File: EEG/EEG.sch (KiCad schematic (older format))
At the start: 46 parts, among them J1 USB_B_Micro, J2 Conn_01x08_Female, J3 Conn_01x08_Female, Q1 SS8050, Q2 SS8050, SW1 SW_Push, SW2 SW_Push, U1 AMS1117-3.3, U2 FT231XS, U3 ESP32-PICO-D4, U4 MAX7219

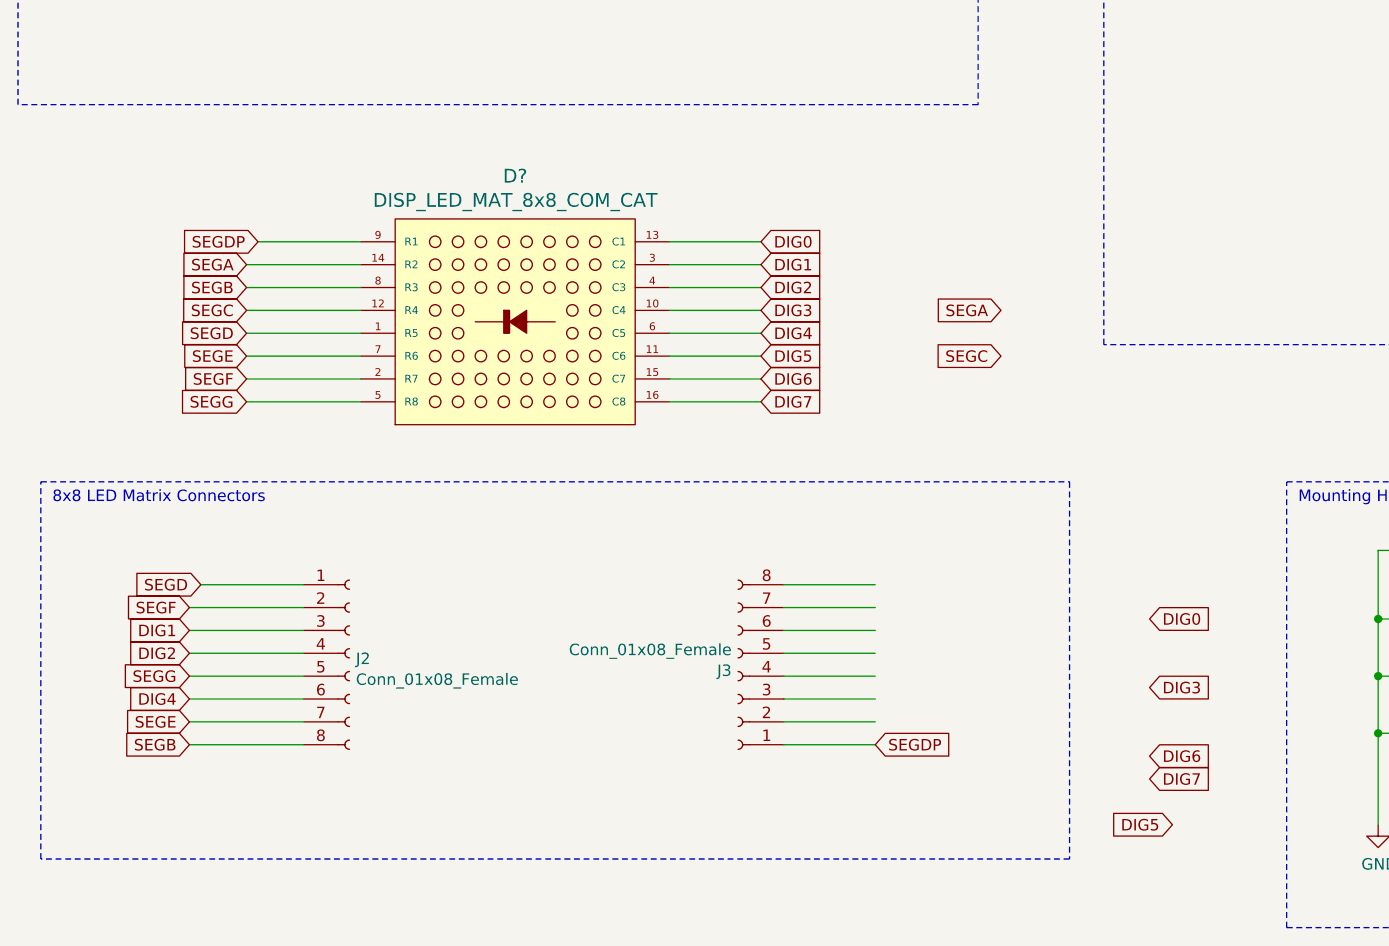
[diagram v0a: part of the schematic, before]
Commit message: updated sch for led conn
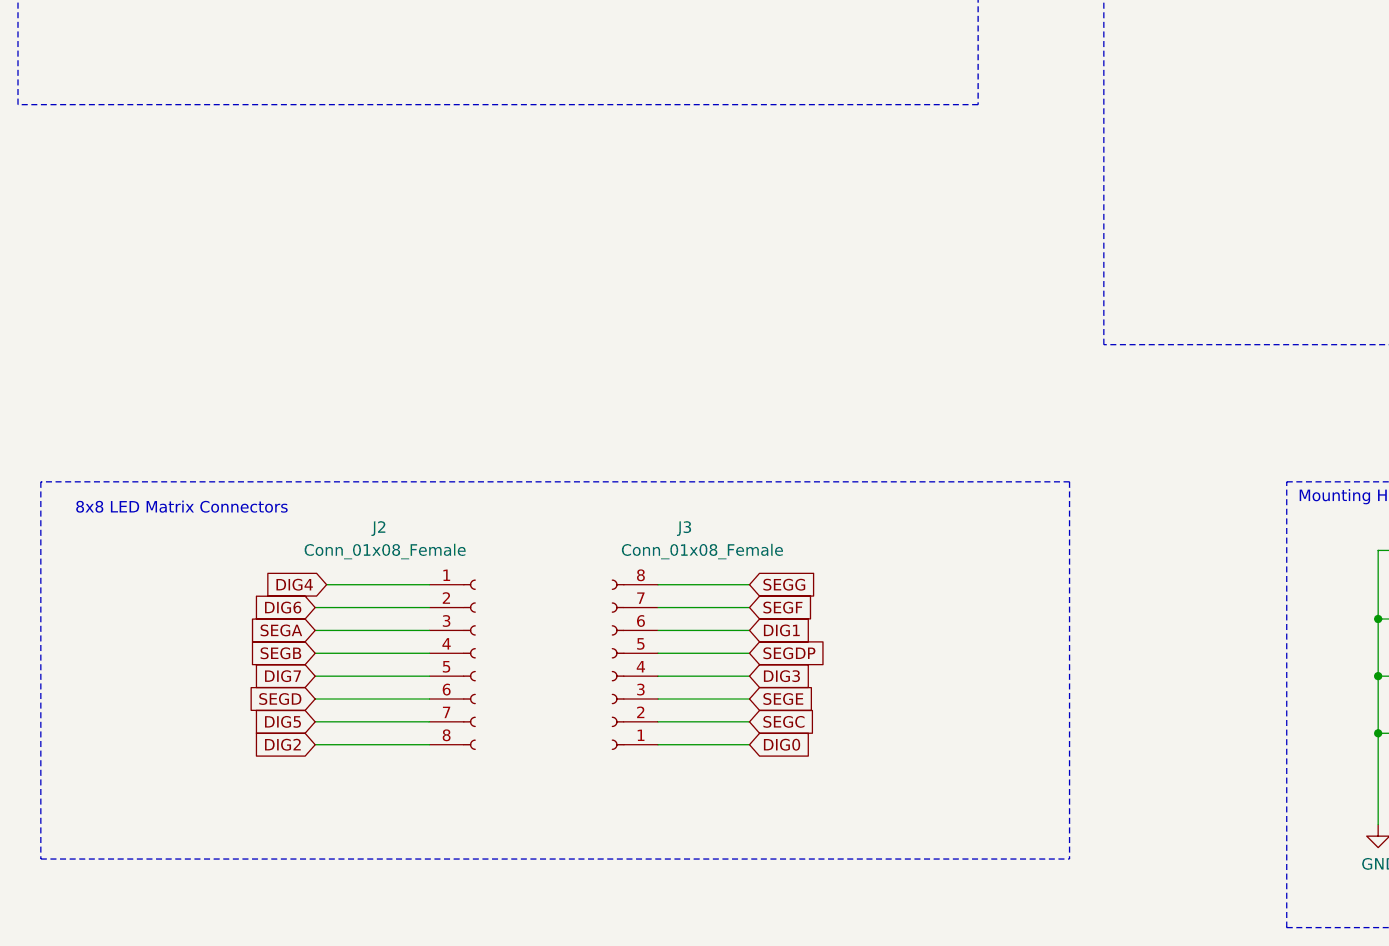
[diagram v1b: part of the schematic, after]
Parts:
- removed D?: DISP_LED_MAT_8x8_COM_CAT, symbol akn_misc:DISP_LED_MAT_8x8_COM_CAT
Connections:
- wire segments 215 -> 199
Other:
- moved on the sheet: J2, J3
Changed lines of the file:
@@
 L Connector:Conn_01x08_Female J3
 U 1 1 604BA9B3
-P 3900 9950
-F 0 "J3" H 3928 9926 50  0000 L CNN
-F 1 "Conn_01x08_Female" H 3928 9835 50  0000 L CNN
-F 2 "Connector_PinSocket_2.54mm:PinSocket_1x08_P2.54mm_Vertical" H 3900 9950 50  0001 C CNN
-F 3 "~" H 3900 9950 50  0001 C CNN
-	1    3900 9950
+P 3350 9950
+F 0 "J3" H 3000 9300 50  0000 L CNN
+F 1 "Conn_01x08_Female" H 2600 9400 50  0000 L CNN
+F 2 "Connector_PinSocket_2.54mm:PinSocket_1x08_P2.54mm_Vertical" H 3350 9950 50  0001 C CNN
+F 3 "~" H 3350 9950 50  0001 C CNN
+	1    3350 9950
 	-1   0    0    1
 $EndComp
@@
 L Connector:Conn_01x08_Female J2
 U 1 1 604BC715
-P 2200 9850
-F 0 "J2" H 2228 9826 50  0000 L CNN
-F 1 "Conn_01x08_Female" H 2228 9735 50  0000 L CNN
-F 2 "Connector_PinSocket_2.54mm:PinSocket_1x08_P2.54mm_Vertical" H 2200 9850 50  0001 C CNN
-F 3 "~" H 2200 9850 50  0001 C CNN
-	1    2200 9850
+P 2750 9850
+F 0 "J2" H 2300 10400 50  0000 L CNN
+F 1 "Conn_01x08_Female" H 2000 10300 50  0000 L CNN
+F 2 "Connector_PinSocket_2.54mm:PinSocket_1x08_P2.54mm_Vertical" H 2750 9850 50  0001 C CNN
+F 3 "~" H 2750 9850 50  0001 C CNN
+	1    2750 9850
 	1    0    0    -1
 $EndComp
@@
 Text Notes 11000 4750 0    50   ~ 0
 MAX7219 LED Matrix Driver
-Wire Notes Line
-	5350 9100 5350 10750
-Wire Notes Line
-	5350 10750 850  10750
-Wire Notes Line
-	850  10750 850  9100
-Wire Notes Line
-	850  9100 5350 9100
-Text Notes 900  9200 0    50   ~ 0
+Text Notes 1000 9250 0    50   ~ 0
 8x8 LED Matrix Connectors
 NoConn ~ 9200 4800
@@
 	1    0    0    -1
 $EndComp
-Text GLabel 1750 8150 0    50   Input ~ 0
+Wire Wire Line
+	3550 10250 3950 10250
+Wire Wire Line
+	3550 10150 3950 10150
+Wire Wire Line
+	3550 10050 3950 10050
+Wire Wire Line
+	3550 9950 3950 9950
+Wire Wire Line
+	3550 9850 3950 9850
+Wire Wire Line
+	3550 9750 3950 9750
+Wire Wire Line
+	3550 9650 3950 9650
+Wire Wire Line
+	3550 9550 3950 9550
+Text GLabel 2050 9950 0    50   Input ~ 0
+DIG7
+Text GLabel 3950 10250 2    50   Input ~ 0
+DIG0
+Text GLabel 2050 9650 0    50   Input ~ 0
+DIG6
+Text GLabel 2050 10150 0    50   Input ~ 0
+DIG5
+Text GLabel 2100 9550 0    50   Input ~ 0
+DIG4
+Text GLabel 3950 9950 2    50   Input ~ 0
+DIG3
+Text GLabel 2050 10250 0    50   Input ~ 0
+DIG2
+Text GLabel 3950 9750 2    50   Input ~ 0
+DIG1
+Text GLabel 3950 9850 2    50   Input ~ 0
+SEGDP
+Text GLabel 3950 9550 2    50   Input ~ 0
+SEGG
+Text GLabel 3950 9650 2    50   Input ~ 0
+SEGF
+Text GLabel 3950 10050 2    50   Input ~ 0
+SEGE
+Text GLabel 2050 10050 0    50   Input ~ 0
+SEGD
+Text GLabel 3950 10150 2    50   Input ~ 0
+SEGC
+Text GLabel 2050 9850 0    50   Input ~ 0
+SEGB
+Text GLabel 2050 9750 0    50   Input ~ 0
 SEGA
-Text GLabel 1750 8250 0    50   Input ~ 0
-SEGB
-Text GLabel 1750 8350 0    50   Input ~ 0
-SEGC
-Text GLabel 1750 8450 0    50   Input ~ 0
-SEGD
-Text GLabel 1750 8550 0    50   Input ~ 0
-SEGE
-Text GLabel 1750 8650 0    50   Input ~ 0
-SEGF
-Text GLabel 1750 8750 0    50   Input ~ 0
-SEGG
-Wire Wire Line
-	1750 8150 2250 8150
-Wire Wire Line
-	1750 8250 2250 8250
-Wire Wire Line
-	1750 8350 2250 8350
-Wire Wire Line
-	1750 8450 2250 8450
-Wire Wire Line
-	1750 8550 2250 8550
-Wire Wire Line
-	1750 8650 2250 8650
-Wire Wire Line
-	1750 8750 2250 8750
-Text GLabel 4000 8150 2    50   Input ~ 0
-DIG1
-Text GLabel 4000 8250 2    50   Input ~ 0
-DIG2
-Text GLabel 4000 8350 2    50   Input ~ 0
-DIG3
-Text GLabel 4000 8450 2    50   Input ~ 0
-DIG4
-Text GLabel 4000 8550 2    50   Input ~ 0
-DIG5
-Text GLabel 4000 8650 2    50   Input ~ 0
-DIG6
-Text GLabel 4000 8050 2    50   Input ~ 0
-DIG0
-Text GLabel 4000 8750 2    50   Input ~ 0
-DIG7
-Wire Wire Line
-	3600 8050 4000 8050
-Wire Wire Line
-	3600 8150 4000 8150
-Wire Wire Line
-	3600 8250 4000 8250
-Wire Wire Line
-	3600 8350 4000 8350
-Wire Wire Line
-	3600 8450 4000 8450
-Wire Wire Line
-	3600 8550 4000 8550
-Wire Wire Line
-	3600 8650 4000 8650
-Wire Wire Line
-	3600 8750 4000 8750
-Wire Wire Line
-	4100 10250 4500 10250
-Wire Wire Line
-	4100 10150 4500 10150
-Wire Wire Line
-	4100 10050 4500 10050
-Wire Wire Line
-	4100 9950 4500 9950
-Wire Wire Line
-	4100 9850 4500 9850
-Wire Wire Line
-	4100 9750 4500 9750
-Wire Wire Line
-	4100 9650 4500 9650
-Wire Wire Line
-	4100 9550 4500 9550
-Text GLabel 5700 10400 2    50   Input ~ 0
-DIG7
-Text GLabel 5700 9700 2    50   Input ~ 0
-DIG0
-Text GLabel 5700 10300 2    50   Input ~ 0
-DIG6
-Text GLabel 5800 10600 0    50   Input ~ 0
-DIG5
-Text GLabel 1500 10050 0    50   Input ~ 0
-DIG4
-Text GLabel 5700 10000 2    50   Input ~ 0
-DIG3
-Text GLabel 1500 9850 0    50   Input ~ 0
-DIG2
-Text GLabel 1500 9750 0    50   Input ~ 0
-DIG1
-Wire Wire Line
-	1550 9550 2000 9550
-Wire Wire Line
-	1500 10250 2000 10250
-Wire Wire Line
-	1500 10150 2000 10150
-Wire Wire Line
-	1500 10050 2000 10050
-Wire Wire Line
-	1500 9950 2000 9950
-Wire Wire Line
-	1500 9850 2000 9850
-Wire Wire Line
-	1500 9750 2000 9750
-Wire Wire Line
-	1500 9650 2000 9650
-Text GLabel 4500 10250 2    50   Input ~ 0
-SEGDP
-Text GLabel 1500 9950 0    50   Input ~ 0
-SEGG
-Text GLabel 1500 9650 0    50   Input ~ 0
-SEGF
-Text GLabel 1500 10150 0    50   Input ~ 0
-SEGE
-Text GLabel 1550 9550 0    50   Input ~ 0
-SEGD
-Text GLabel 5050 8550 0    50   Input ~ 0
-SEGC
-Text GLabel 1500 10250 0    50   Input ~ 0
-SEGB
-Text GLabel 5050 8350 0    50   Input ~ 0
-SEGA
-Text GLabel 1800 8050 0    50   Input ~ 0
-SEGDP
-$Comp
-L akn_misc:DISP_LED_MAT_8x8_COM_CAT D?
-U 1 1 60652E1D
-P 2250 8850
-F 0 "D?" H 2925 9937 60  0000 C CNN
-F 1 "DISP_LED_MAT_8x8_COM_CAT" H 2925 9831 60  0000 C CNN
-F 2 "" H 2350 8800 60  0000 C CNN
-F 3 "" H 2350 8800 60  0000 C CNN
-	1    2250 8850
-	1    0    0    -1
-$EndComp
-Wire Wire Line
-	1800 8050 2250 8050
+Wire Wire Line
+	2050 9650 2550 9650
+Wire Wire Line
+	2050 9750 2550 9750
+Wire Wire Line
+	2050 9850 2550 9850
+Wire Wire Line
+	2050 9950 2550 9950
+Wire Wire Line
+	2050 10050 2550 10050
+Wire Wire Line
+	2050 10150 2550 10150
+Wire Wire Line
+	2050 10250 2550 10250
+Wire Wire Line
+	2100 9550 2550 9550
+Wire Notes Line
+	5350 9100 850  9100
+Wire Notes Line
+	850  9100 850  10750
+Wire Notes Line
+	850  10750 5350 10750
+Wire Notes Line
+	5350 9100 5350 10750
 $EndSCHEMATC

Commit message: Finished routing
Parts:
- added D3: LED, LED_SMD:LED_1206_3216Metric_Pad1.42x1.75mm_HandSolder, symbol Device:LED
- added R12: 2K, Resistor_SMD:R_1206_3216Metric_Pad1.30x1.75mm_HandSolder, symbol Device:R_Small_US
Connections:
- net GND: now also R12.2
- net at U3.15 (IO26): now also D3.2 (A)
- new net: D3.1 (K), R12.1
- no-connect marks 41 -> 40
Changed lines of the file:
@@
 NoConn ~ 9200 6500
 NoConn ~ 9200 6700
-NoConn ~ 9200 6800
 NoConn ~ 9200 6900
 NoConn ~ 9200 7000
@@
 Wire Notes Line
 	5350 9100 5350 10750
+$Comp
+L Device:R_Small_US R12
+U 1 1 60531F6E
+P 9850 7350
+F 0 "R12" H 9918 7396 50  0000 L CNN
+F 1 "2K" H 9918 7305 50  0000 L CNN
+F 2 "Resistor_SMD:R_1206_3216Metric_Pad1.30x1.75mm_HandSolder" H 9850 7350 50  0001 C CNN
+F 3 "~" H 9850 7350 50  0001 C CNN
+	1    9850 7350
+	1    0    0    -1
+$EndComp
+$Comp
+L Device:LED D3
+U 1 1 60532570
+P 9850 7050
+F 0 "D3" V 9889 6932 50  0000 R CNN
+F 1 "LED" V 9798 6932 50  0000 R CNN
+F 2 "LED_SMD:LED_1206_3216Metric_Pad1.42x1.75mm_HandSolder" H 9850 7050 50  0001 C CNN
+F 3 "~" H 9850 7050 50  0001 C CNN
+	1    9850 7050
+	0    -1   -1   0
+$EndComp
+Wire Wire Line
+	9850 7200 9850 7250
+Wire Wire Line
+	9850 7450 9850 7750
+Wire Wire Line
+	9850 6800 9850 6900
+$Comp
+L power:GND #PWR?
+U 1 1 6053257E
+P 9850 7750
+F 0 "#PWR?" H 9850 7500 50  0001 C CNN
+F 1 "GND" H 9855 7577 50  0000 C CNN
+F 2 "" H 9850 7750 50  0001 C CNN
+F 3 "" H 9850 7750 50  0001 C CNN
+	1    9850 7750
+	1    0    0    -1
+$EndComp
+Wire Wire Line
+	9200 6800 9850 6800
 $EndSCHEMATC

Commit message: generated gerbers
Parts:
- R3, R4, R7: value 2K -> 10k
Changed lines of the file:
@@
 P 4600 1950
 F 0 "R4" H 4668 1996 50  0000 L CNN
-F 1 "2K" H 4668 1905 50  0000 L CNN
+F 1 "10k" H 4668 1905 50  0000 L CNN
 F 2 "Resistor_SMD:R_1206_3216Metric_Pad1.30x1.75mm_HandSolder" H 4600 1950 50  0001 C CNN
 F 3 "~" H 4600 1950 50  0001 C CNN
@@
 P 13850 2500
 F 0 "R7" H 13918 2546 50  0000 L CNN
-F 1 "2K" H 13918 2455 50  0000 L CNN
+F 1 "10k" H 13918 2455 50  0000 L CNN
 F 2 "Resistor_SMD:R_1206_3216Metric_Pad1.30x1.75mm_HandSolder" H 13850 2500 50  0001 C CNN
 F 3 "~" H 13850 2500 50  0001 C CNN
@@
 P 13850 1700
 F 0 "R3" H 13918 1746 50  0000 L CNN
-F 1 "2K" H 13918 1655 50  0000 L CNN
+F 1 "10k" H 13918 1655 50  0000 L CNN
 F 2 "Resistor_SMD:R_1206_3216Metric_Pad1.30x1.75mm_HandSolder" H 13850 1700 50  0001 C CNN
 F 3 "~" H 13850 1700 50  0001 C CNN
